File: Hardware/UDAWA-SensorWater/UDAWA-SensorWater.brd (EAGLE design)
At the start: 160 x 100 mm, 7 parts

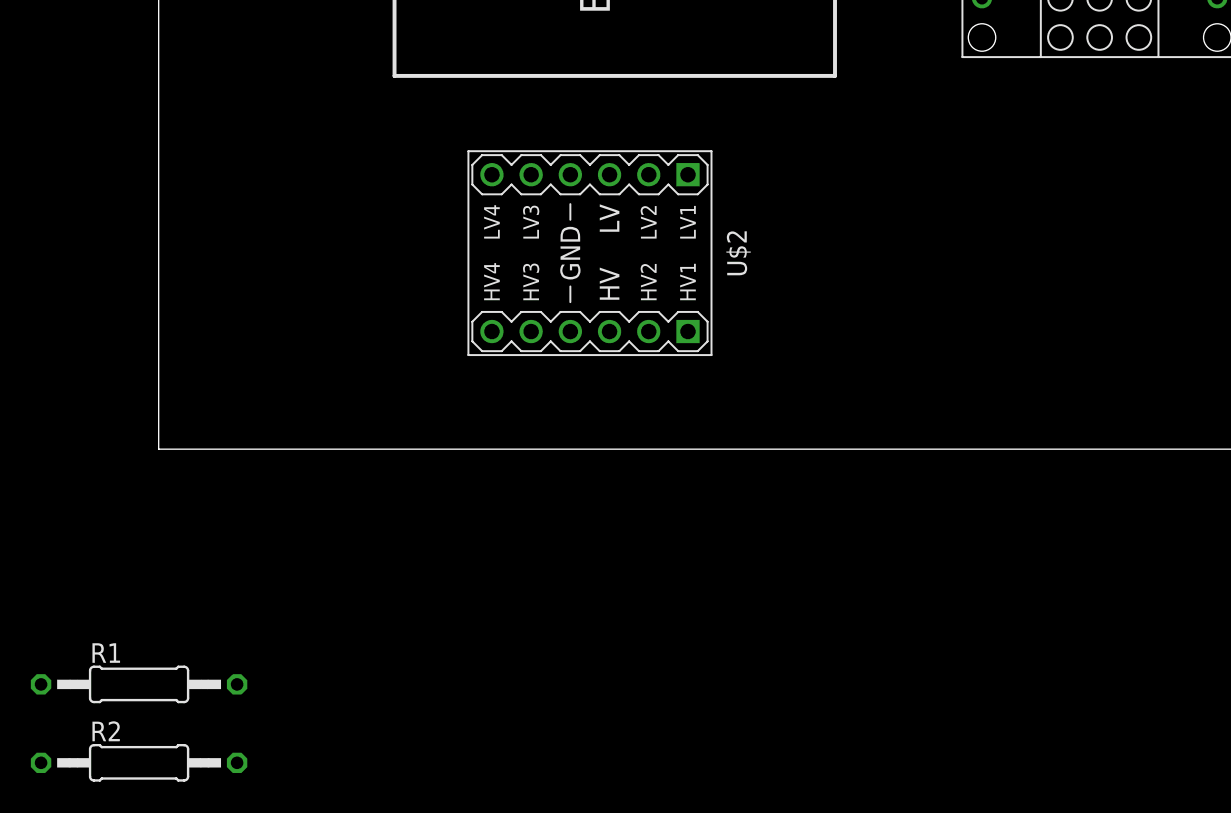
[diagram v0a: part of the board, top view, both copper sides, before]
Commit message: Menambahkan Terminal Block untuk koneksi ke Sensor TDS dan Sensor DS18B20 dan Wiring sesuai diagram di gambar #6
Menambahkan Terminal Block untuk koneksi ke Sensor TDS dan Sensor DS18B20 dan Wiring sesuai diagram di gambar #6
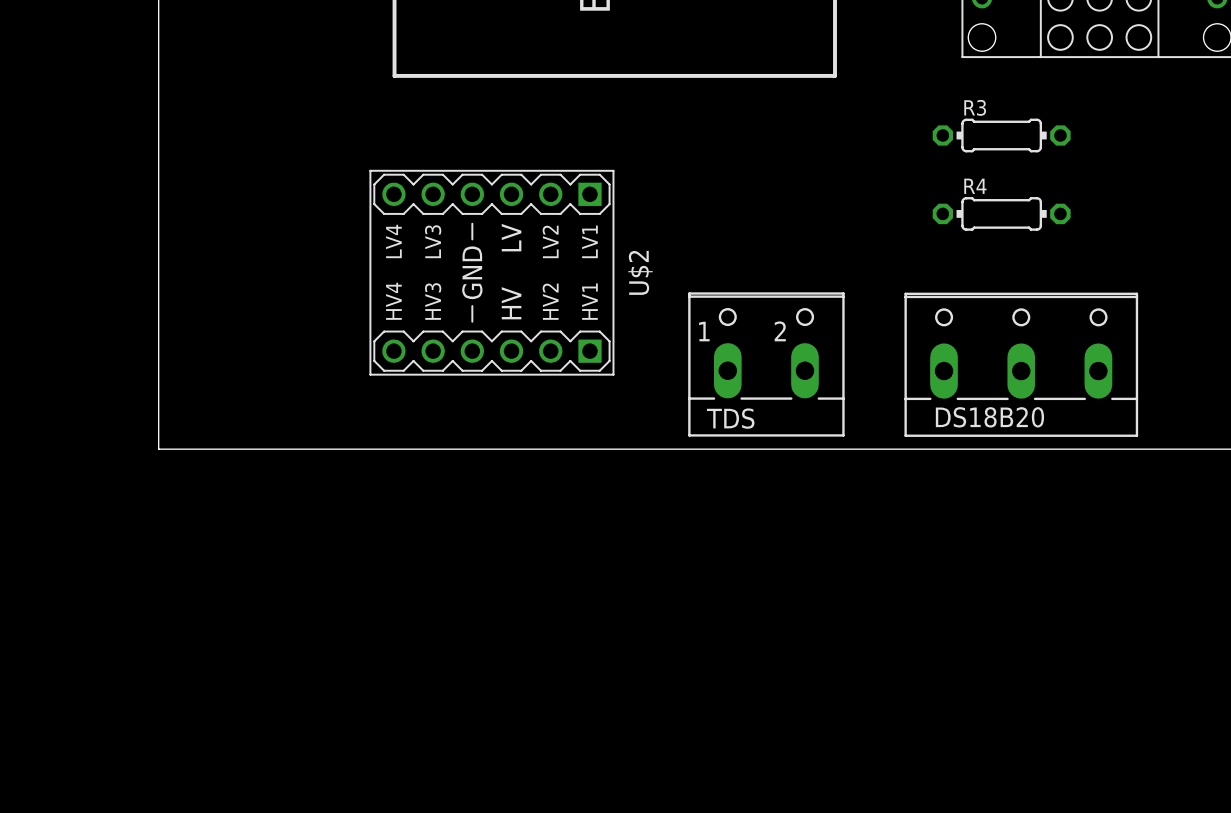
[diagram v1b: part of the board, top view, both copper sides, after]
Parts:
- removed R1: 4.7K, rcl:0207/12
- removed R2: (no value), rcl:0207/12
- added DS18B20: (no value), con-wago-500:W237-103
- added R3: 4.7K, rcl:0204/7
- added R4: 1K, rcl:0204/7
- added TDS: (no value), con-wago-500:W237-102
- moved U$2 6.48 mm to (21.6, 11.4)
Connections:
- net 3V3/LV renamed 3V3
- net HV1/RX renamed HV1
- net HV2/TX renamed HV2
- net RX/LV2 renamed LV2
- net TX/LV1 renamed LV1
- removed net GND1: U$1.GND@2, U$2.J1.4
- removed net GND2: ARDUINO_NANO1.19, U$2.J2.4
- removed net HV/5V: ARDUINO_NANO1.12, U$2.J2.3
- new net A0: ARDUINO_NANO1.4, R4.1, TDS.1
- new net A1: ARDUINO_NANO1.5, R4.2
- new net A2: ARDUINO_NANO1.6, TDS.2
- new net D2: ARDUINO_NANO1.20, DS18B20.2, R3.2
- net 5V: now also ARDUINO_NANO1.12, DS18B20.3, R3.1, U$2.J2.3
- net GND: now also ARDUINO_NANO1.19, DS18B20.1, U$1.GND@2, U$2.J1.4, U$2.J2.4

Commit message: First working version of Water Sensor
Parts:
- removed DS18B20: (no value), con-wago-500:W237-103
- added D_STEMP, P_STEMP: (no value), con-wago-500:W237-102
- moved U$2 52.8 mm to (68.6, 35.6), turned to 90 degrees
- moved TDS 48.0 mm to (10.2, 44.5), turned to 270 degrees
- moved R3 46.0 mm to (19.1, 49.5)
- moved U$1 39.5 mm to (68.6, 47.0), turned to 90 degrees
- moved ARDUINO_NANO1 26.7 mm to (34.3, 44.5), turned to 90 degrees
- moved R4 23.4 mm to (36.8, 30.5), turned to 90 degrees
- moved 220V 10.9 mm to (10.2, 83.8)
- moved HLK1 6.35 mm to (34.3, 83.8)
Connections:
- net 5V: now also P_STEMP.2; no longer DS18B20.3
- net D2: now also D_STEMP.1, D_STEMP.2; no longer DS18B20.2
- net GND: now also P_STEMP.1; no longer DS18B20.1
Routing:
- net HV1: track 0.00 -> 225.3 mm, vias 0 -> 4
- net HV2: track 0.00 -> 209.8 mm, vias 0 -> 4
- net 5V: track 22.5 -> 221.9 mm
- net GND: track 41.9 -> 186.1 mm, vias 0 -> 2
- net A2: track 0.00 -> 75.2 mm
- net LV1: track 0.00 -> 62.1 mm
- net A0: track 0.00 -> 58.7 mm
- net LV2: track 0.00 -> 49.1 mm
- net D2: track 0.00 -> 27.7 mm
- net 3V3: track 0.00 -> 22.8 mm
- net A1: track 0.00 -> 5.08 mm
- net AC2: track 14.7 -> 10.7 mm
- net AC1: track 12.8 -> 10.7 mm
- added copper zone on layer 1, net GND
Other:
- board size 160 x 100 mm -> 100.3 x 92.4 mm
- board text added: "FTI Undiknas"
- board text added: "HW Ver.1"
- board text added: "UDAWA"
- board text added: "Universal Digital Agriculture Watering Assistant"
- board text added: "Water Sensor"
- board text added: "github.com/NarinLab/Udawa"

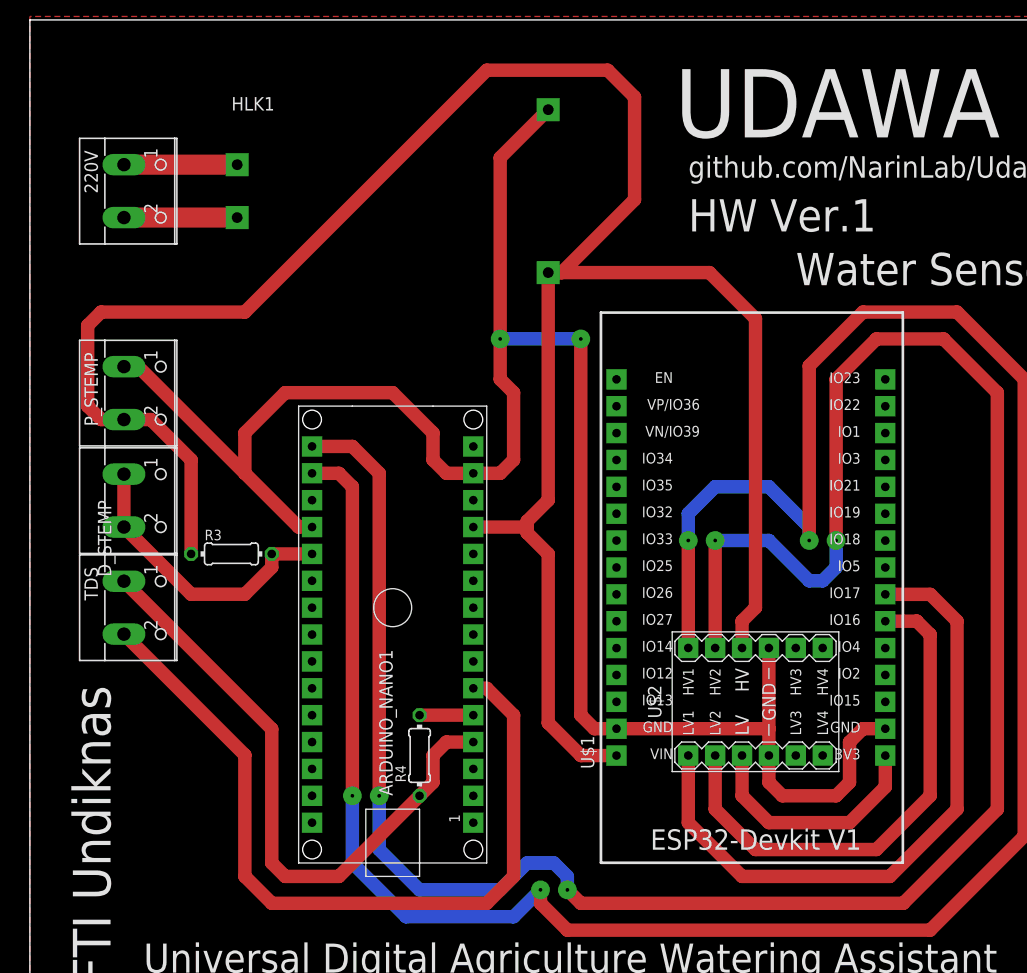
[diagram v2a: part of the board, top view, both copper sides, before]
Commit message: Revisi terminal catu daya. Solar panel support.
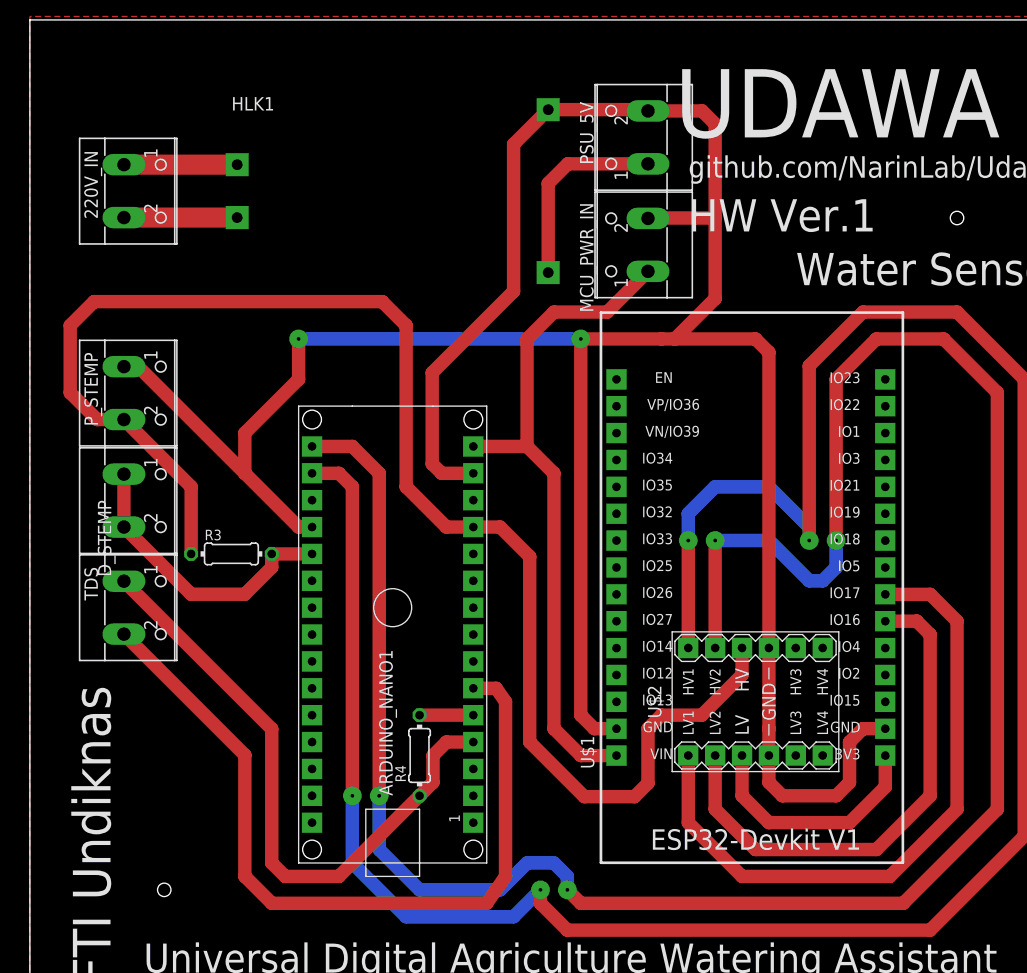
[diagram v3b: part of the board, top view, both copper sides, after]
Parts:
- added MCU_PWR_IN, PSU_5V: (no value), con-wago-500:W237-102
- renumbered 220V to 220V_IN
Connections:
- new net 5V_NANO: ARDUINO_NANO1.12, P_STEMP.2, R3.1, U$2.J2.3
- net 5V: now also PSU_5V.1; no longer ARDUINO_NANO1.12, P_STEMP.2, R3.1, U$1.VIN, U$2.J2.3
- net GND: now also MCU_PWR_IN.2, PSU_5V.2
- net VIN: now also MCU_PWR_IN.1, U$1.VIN
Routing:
- net 5V: track 221.9 -> 18.6 mm
- net 5V_NANO: track 0.00 -> 141.2 mm
- net GND: track 186.1 -> 267.3 mm
- net VIN: track 0.00 -> 64.0 mm
